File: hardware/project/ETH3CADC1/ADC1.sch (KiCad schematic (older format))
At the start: 50 parts, among them U201 DG211, U202 DG211B, U203 OPA2192, U204 DG419DY, U205 OPA140, U206 LT5400-100k-100k, U207 LT5400-5k-1k, U208 OPA177, U209 OPA140, U210 LT5400-10k-10k, U211 OPA192, U212 LM311

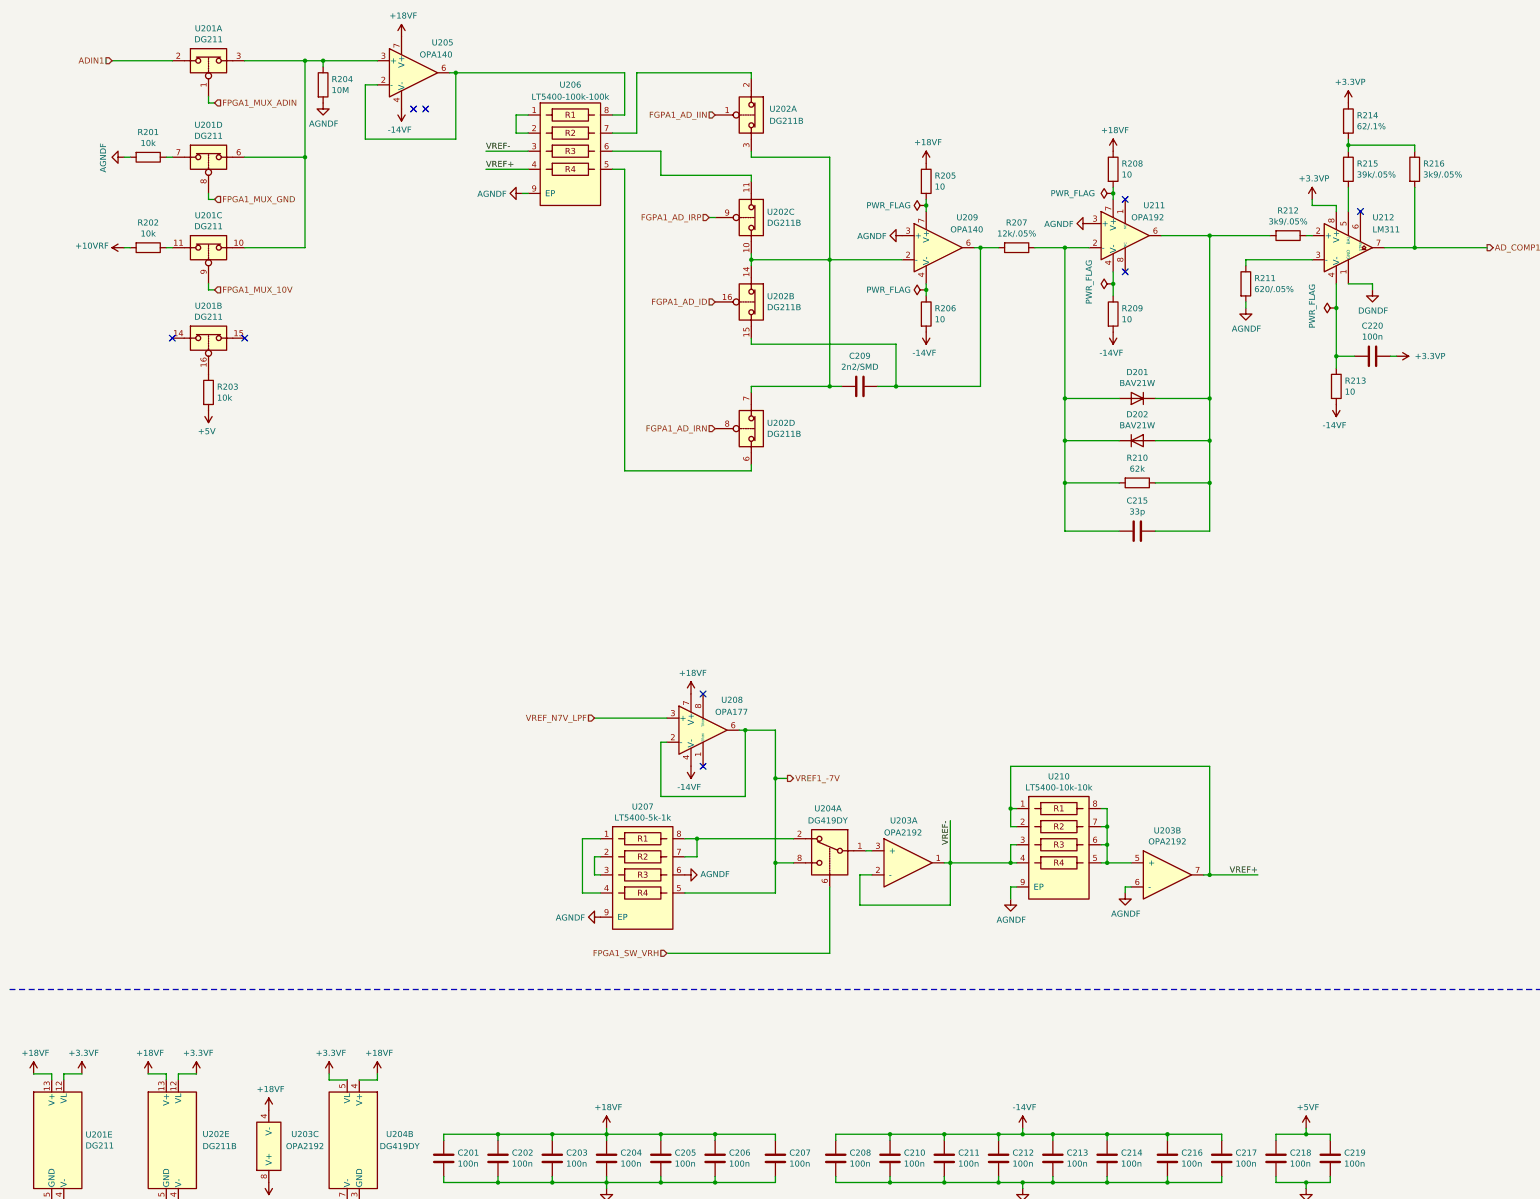
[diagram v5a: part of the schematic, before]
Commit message: Added SDRAM to the linker file.
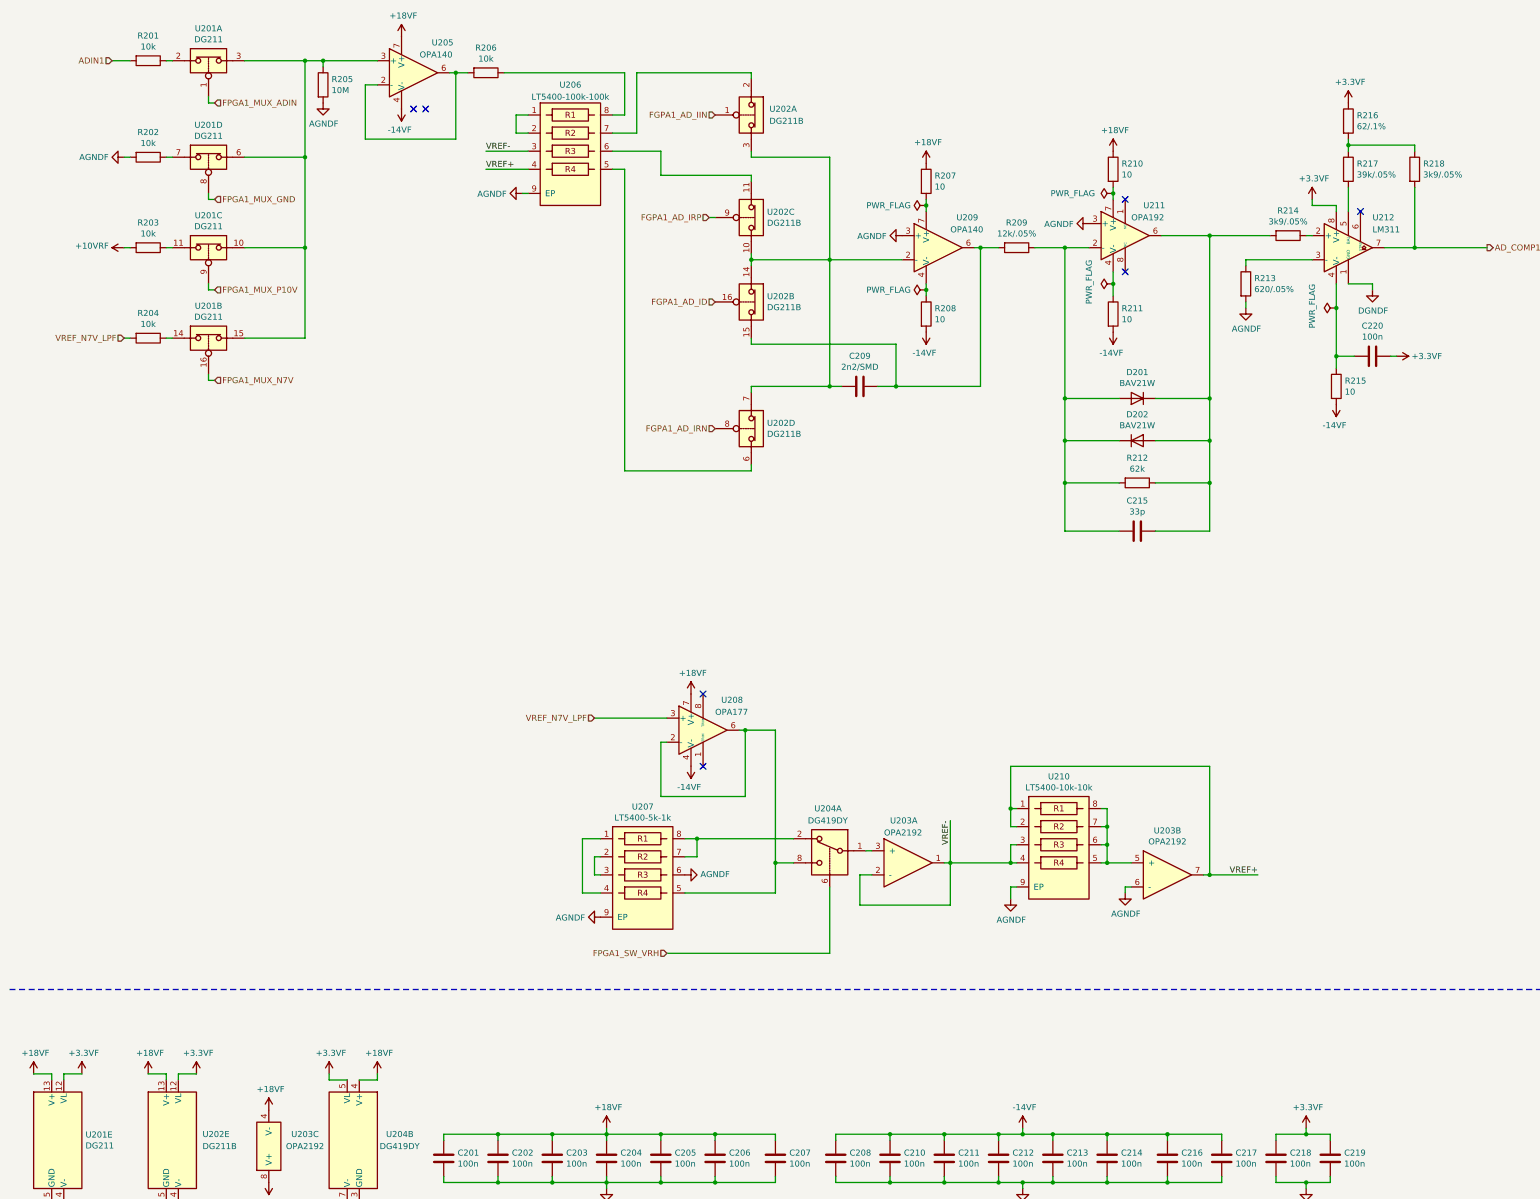
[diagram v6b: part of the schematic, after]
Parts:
- removed R203: 10k, Resistor_SMD:R_0402_1005Metric_Pad0.72x0.64mm_HandSolder, symbol Device:R
- added R201, R204, R206: 10k, Resistor_SMD:R_0402_1005Metric_Pad0.72x0.64mm_HandSolder, symbol Device:R
- renumbered R201 to R202, R202 to R203, R204 to R205, R205 to R207, R206 to R208, R207 to R209, R208 to R210, R209 to R211, R210 to R212, R211 to R213, R212 to R214, R213 to R215, R214 to R216, R215 to R217, R216 to R218
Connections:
- net +3.3VP is gone; now on net +3.3VF: C220.1, R216.1, U212.8 (V+)
- net +5VF is gone; now on net +3.3VF: C218.1, C219.1
- net ADIN1: now also R201.2; no longer U201.2
- net VREF_N7V_LPF: now also R204.2
- net at U205.2 (-), U205.6: now also R206.2; no longer U206.8
- net at R205.1, U201.10, U201.3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: now also U201.15
- net at U201.14: now also R204.1
- net FPGA1_MUX_N7V: now reaches U201.16
- net FPGA1_MUX_10V renamed FPGA1_MUX_P10V
- net VREF1_-7V: no longer names the net of U204.8, U207.5, U208.2 (-), U208.6
- new net: R206.1, U206.8
- new net: R201.1, U201.2
- no-connect marks 9 -> 7

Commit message: PCB and software development.
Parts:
- added R219: 0, Resistor_SMD:R_0402_1005Metric_Pad0.72x0.64mm_HandSolder, symbol Device:R
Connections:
- net at R206.2, U205.2 (-), U205.6: now also R219.1
- net at R205.1, U201.10, U201.15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: now also R219.2
- no-connect marks 7 -> 5
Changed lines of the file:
@@
 U 1 1 5FE103EF
 P 3850 1500
-F 0 "U205" H 4000 1750 50  0000 L CNN
-F 1 "OPA140" H 3900 1650 50  0000 L CNN
+F 0 "U205" H 3900 1750 50  0000 L CNN
+F 1 "OPA140" H 3850 1650 50  0000 L CNN
 F 2 "Package_SO:SOIC-8_3.9x4.9mm_P1.27mm" H 3900 1550 50  0001 C CNN
 F 3 "" H 4000 1650 50  0001 C CNN
@@
 	-1   0    0    1
 $EndComp
-NoConn ~ 3850 1800
-NoConn ~ 3950 1800
 Wire Wire Line
 	3550 1600 3450 1600
@@
 	3100 1450 3100 1400
 Wire Wire Line
-	3100 1400 3550 1400
+	3100 1400 3450 1400
 $Comp
 L ETH3CDAQ1:AGNDF #PWR?
@@
 Wire Wire Line
 	4600 1500 5600 1500
+$Comp
+L Device:R R219
+U 1 1 5FFF3BC5
+P 3800 900
+F 0 "R219" V 3593 900 50  0000 C CNN
+F 1 "0" V 3684 900 50  0000 C CNN
+F 2 "Resistor_SMD:R_0402_1005Metric_Pad0.72x0.64mm_HandSolder" V 3730 900 50  0001 C CNN
+F 3 "~" H 3800 900 50  0001 C CNN
+	1    3800 900
+	0    1    1    0
+$EndComp
+Wire Wire Line
+	3650 900  3450 900
+Wire Wire Line
+	3450 900  3450 1400
+Connection ~ 3450 1400
+Wire Wire Line
+	3450 1400 3550 1400
+Wire Wire Line
+	3950 900  4200 900
+Wire Wire Line
+	4200 900  4200 1500
 $EndSCHEMATC

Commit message: PCB layout
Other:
- moved on the sheet: U203A, U203B, U204A, U207, U208, U210
